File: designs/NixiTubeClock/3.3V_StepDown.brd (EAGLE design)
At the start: 31 x 32 mm, 10 parts, among them IC1 TPS62160DGKR, J1 S2B-PH-SM4, J2 S2B-PH-SM4

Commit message: added parts for nixi clock final check during the week
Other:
- board size 31 x 32 mm -> 31 x 34 mm
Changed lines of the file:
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@@
 <setting verticaltext="up"/>
 </settings>
-<grid distance="1" unitdist="mm" unit="mm" style="lines" multiple="1" display="yes" altdistance="5" altunitdist="mil" altunit="mil"/>
+<grid distance="2" unitdist="mm" unit="mm" style="lines" multiple="1" display="yes" altdistance="5" altunitdist="mil" altunit="mil"/>
 <layers>
 <layer number="1" name="Top" color="4" fill="1" visible="yes" active="yes"/>
@@
 </layers>
 <board>
-<fusionsync huburn="a.cGVyc29uYWw6dWUyYTNmMDU1" projecturn="a.cGVyc29uYWw6dWUyYTNmMDU1IzIwMTgxMjEwMTY0OTQ5MjI2" f3durn="urn:adsk.wipprod:dm.lineage:qr5fd7wmTYGYkqGqhFxAAQ" pcbguid="ed1bca21-045a-418e-931a-820db0e3dc27" lastpulledtime="" lastsyncedchangeguid="ae491c87-77c9-2377-a230-266f3260ef8a"/>
+<fusionsync huburn="a.cGVyc29uYWw6dWUyYTNmMDU1" projecturn="a.cGVyc29uYWw6dWUyYTNmMDU1IzIwMTgxMjEwMTY0OTQ5MjI2" f3durn="urn:adsk.wipprod:dm.lineage:qr5fd7wmTYGYkqGqhFxAAQ" pcbguid="ed1bca21-045a-418e-931a-820db0e3dc27" lastpulledtime="" lastsyncedchangeguid="2cda2d61-7268-cf4c-ad3c-c233fa6ebd5d"/>
 <plain>
 <text x="3.58" y="7.825" size="0.6096" layer="25">C1</text>
-<text x="2.405" y="21.225" size="1.016" layer="25" ratio="20" rot="R90">Gnd</text>
-<text x="0.675" y="21.225" size="1.016" layer="25" ratio="20" rot="R90">IOUT</text>
-<text x="25.025" y="21.225" size="1.016" layer="25" ratio="20" rot="R90">Gnd</text>
-<text x="23.295" y="21.225" size="1.016" layer="25" ratio="20" rot="R90">VIN</text>
-<text x="8.755" y="3.945" size="0.6096" layer="25" ratio="20" rot="R90">VIN</text>
-<text x="11.295" y="3.945" size="0.6096" layer="25" ratio="20" rot="R90">GND</text>
-<text x="13.835" y="3.945" size="0.6096" layer="25" ratio="20" rot="R90">GND</text>
-<text x="16.375" y="3.945" size="0.6096" layer="25" ratio="20" rot="R90">IOUT</text>
+<text x="0.405" y="21.225" size="1.016" layer="25" ratio="20" rot="R90">Gnd</text>
+<text x="2.675" y="21.225" size="1.016" layer="25" ratio="20" rot="R90">IOUT</text>
+<text x="23.025" y="21.225" size="1.016" layer="25" ratio="20" rot="R90">Gnd</text>
+<text x="25.295" y="21.225" size="1.016" layer="25" ratio="20" rot="R90">VIN</text>
+<text x="8.755" y="3.945" size="1.016" layer="25" ratio="20" rot="R90">VIN</text>
+<text x="11.295" y="3.945" size="1.016" layer="25" ratio="20" rot="R90">GND</text>
+<text x="13.835" y="3.945" size="1.016" layer="25" ratio="20" rot="R90">GND</text>
+<text x="16.375" y="3.945" size="1.016" layer="25" ratio="20" rot="R90">IOUT</text>
 <rectangle x1="22.99481875" y1="15.91635" x2="23.13198125" y2="15.92905" layer="22"/>
 <rectangle x1="19.00701875" y1="15.92905" x2="19.04258125" y2="15.94175" layer="22"/>
@@
 <dimension x1="24" y1="30" x2="23.765" y2="0" x3="33.5" y3="15" textsize="1.778" layer="47" dtype="vertical"/>
 <dimension x1="0" y1="1" x2="12.5" y2="2" x3="6.25" y3="-3.5" textsize="1.778" layer="47" dtype="horizontal"/>
-<hole x="0" y="2.5" drill="2.8"/>
-<hole x="25" y="2.5" drill="2.8"/>
+<hole x="0" y="0.5" drill="2.8"/>
+<hole x="25" y="0.5" drill="2.8"/>
 <hole x="0" y="27.5" drill="2.8"/>
 <hole x="25" y="27.5" drill="2.8"/>
@@
 <wire x1="22.5" y1="31" x2="26" y2="31" width="0.0762" layer="20"/>
 <wire x1="26" y1="31" x2="28" y2="29" width="0.0762" layer="20" curve="-90"/>
-<wire x1="28" y1="29" x2="28" y2="1" width="0.0762" layer="20"/>
-<wire x1="28" y1="1" x2="26" y2="-1" width="0.0762" layer="20" curve="-90"/>
-<wire x1="26" y1="-1" x2="-1" y2="-1" width="0.0762" layer="20"/>
-<wire x1="-1" y1="-1" x2="-3" y2="1" width="0.0762" layer="20" curve="-90"/>
-<wire x1="-3" y1="1" x2="-3" y2="29" width="0.0762" layer="20"/>
+<wire x1="28" y1="29" x2="28" y2="-1" width="0.0762" layer="20"/>
+<wire x1="28" y1="-1" x2="26" y2="-3" width="0.0762" layer="20" curve="-90"/>
+<wire x1="26" y1="-3" x2="-1" y2="-3" width="0.0762" layer="20"/>
+<wire x1="-1" y1="-3" x2="-3" y2="-1" width="0.0762" layer="20" curve="-90"/>
+<wire x1="-3" y1="-1" x2="-3" y2="29" width="0.0762" layer="20"/>
 <wire x1="-3" y1="29" x2="-1" y2="31" width="0.0762" layer="20" curve="-90"/>
 <wire x1="-1" y1="31" x2="2.5" y2="31" width="0.0762" layer="20"/>
@@
 <vertex x="7.3025" y="9.4375"/>
 <vertex x="9.39" y="7.35"/>
-<vertex x="9.39" y="-1"/>
+<vertex x="9.39" y="-3"/>
+<vertex x="-1" y="-3" curve="-90"/>
 <vertex x="-3" y="-1"/>
 </polygon>
@@
 <vertex x="13.335" y="9.12"/>
 <vertex x="15.24" y="7.215"/>
-<vertex x="15.24" y="-1"/>
+<vertex x="15.24" y="-3"/>
+<vertex x="26.0825" y="-3" curve="90"/>
 <vertex x="28.0825" y="-1"/>
 <vertex x="28.0825" y="31.3525"/>
@@
 <vertex x="7.9375" y="9.755"/>
 <vertex x="10.025" y="7.6675"/>
-<vertex x="10.025" y="-1"/>
-<vertex x="14.605" y="-1"/>
+<vertex x="10.025" y="-3"/>
+<vertex x="14.605" y="-3"/>
 <vertex x="14.605" y="6.8975"/>
 <vertex x="13.0175" y="8.485"/>
@@
 <vertex x="5.08" y="6.985"/>
 <vertex x="27.765" y="6.985"/>
-<vertex x="27.765" y="-1"/>
+<vertex x="27.765" y="-1" curve="-90"/>
+<vertex x="25.765" y="-3"/>
+<vertex x="-1" y="-3" curve="-90"/>
 <vertex x="-3" y="-1"/>
 <vertex x="-3" y="30.845"/>

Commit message: started work on mainboard
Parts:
- removed J1, J2: S2B-PH-SM4, CommonParts:JST_S2B-PH-SM4-TB(LF)(SN)
- moved C2 1.41 mm to (8.14, 17.0)
- moved C1 1.41 mm to (2.81, 12.0)
- moved IC1 1.41 mm to (8.14, 13.3)
- moved L1 1.41 mm to (19.5, 16.5)
- moved R1 1.41 mm to (18.8, 10.2)
- moved R2 1.41 mm to (14.0, 10.2)
- moved R3 1.41 mm to (10.4, 10.2)
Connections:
- net AGND: no longer J1.2, J2.2
- net IOUT: no longer J2.1
- net VIN: no longer J1.1
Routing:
- net VIN: track 52.6 -> 19.5 mm, vias 2 -> 0
- net AGND: track 55.0 -> 29.9 mm, vias 2 -> 0
- net IOUT: track 54.5 -> 48.6 mm
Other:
- board size 31 x 34 mm -> 26 x 28 mm
- board text removed: "Gnd"

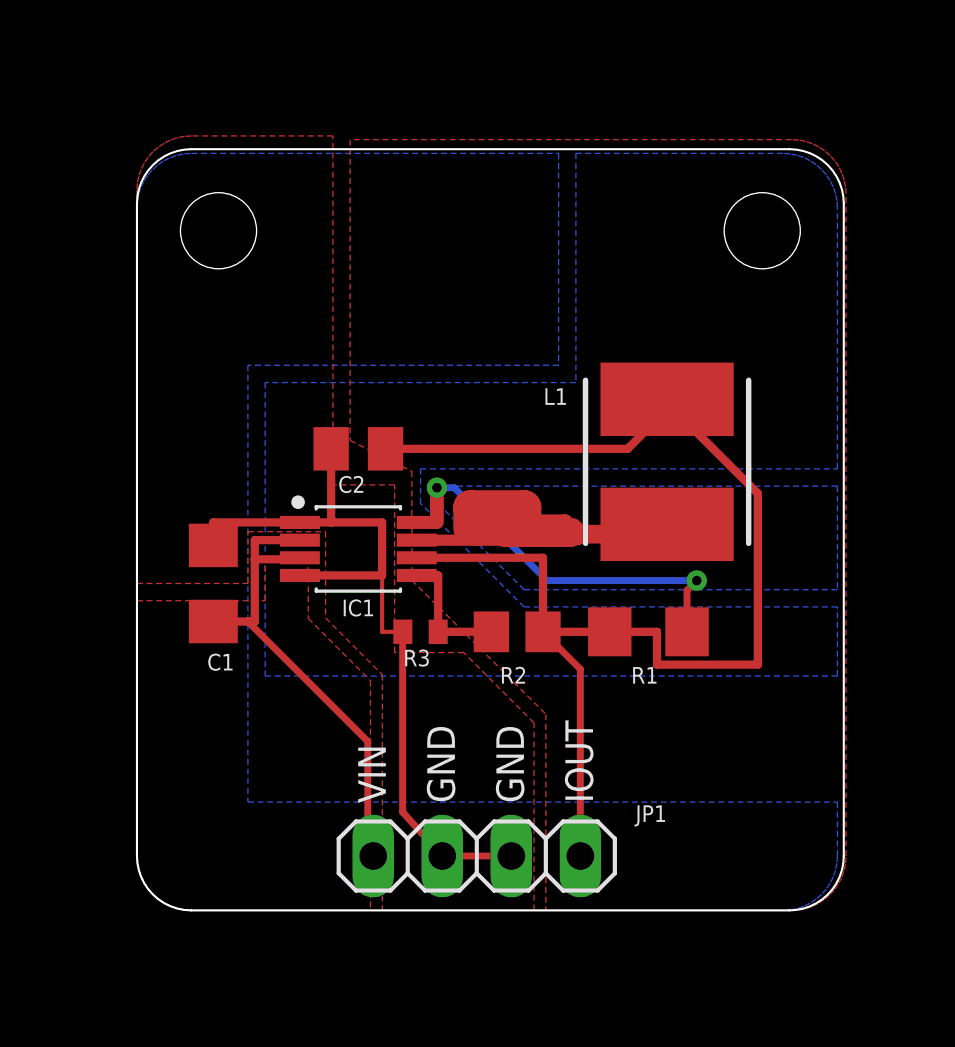
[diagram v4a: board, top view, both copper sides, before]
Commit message: added pinout on mainboard
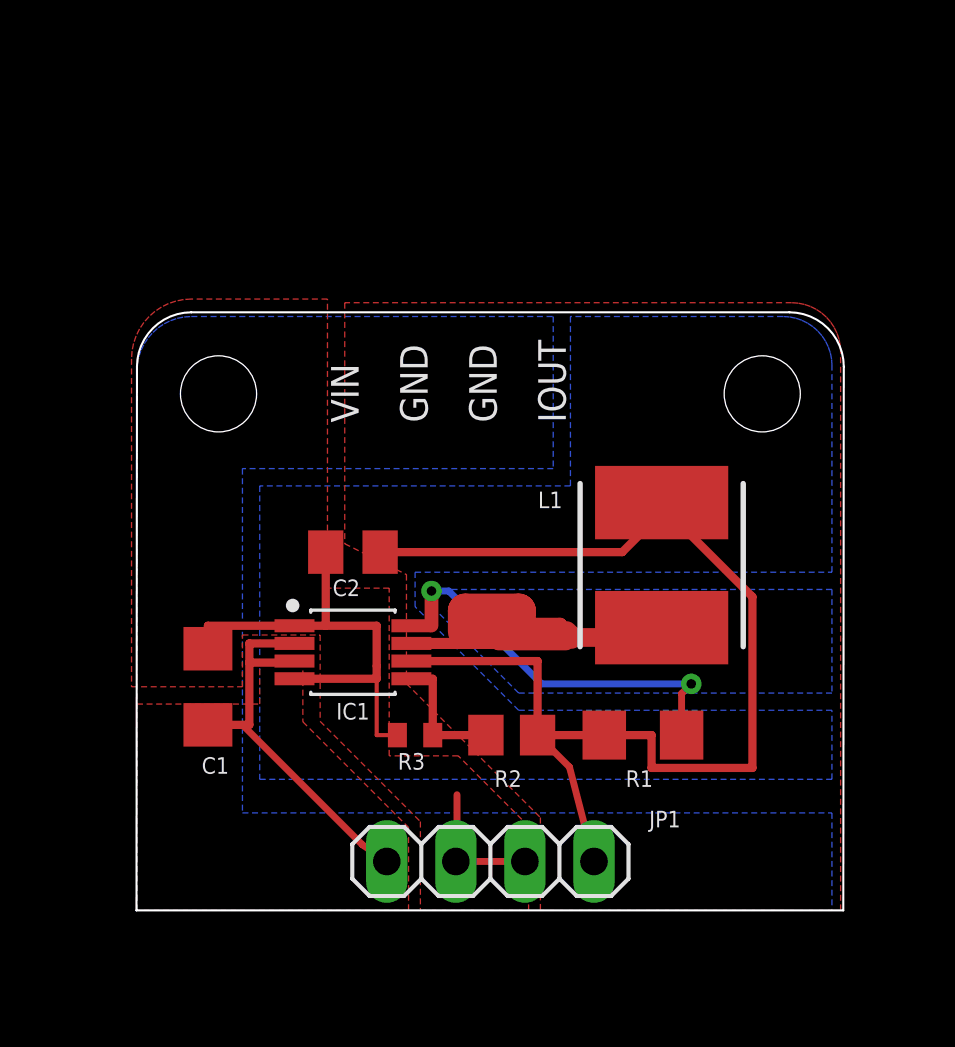
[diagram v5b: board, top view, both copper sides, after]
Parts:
- moved C1 3.81 mm to (2.61, 8.22)
- moved C2 3.81 mm to (7.94, 13.2)
- moved IC1 3.81 mm to (7.94, 9.49)
- moved L1 3.81 mm to (19.3, 12.7)
- moved R1 3.81 mm to (18.6, 6.45)
- moved R2 3.81 mm to (13.8, 6.45)
- moved R3 3.81 mm to (10.2, 6.45)
- moved JP1 0.54 mm to (13.0, 1.80)
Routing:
- net AGND: track 29.9 -> 23.6 mm
- net IOUT: track 48.6 -> 45.0 mm
- net VIN: track 19.5 -> 16.3 mm
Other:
- board size 26 x 28 mm -> 26 x 22 mm

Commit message: integrated T/H sensor
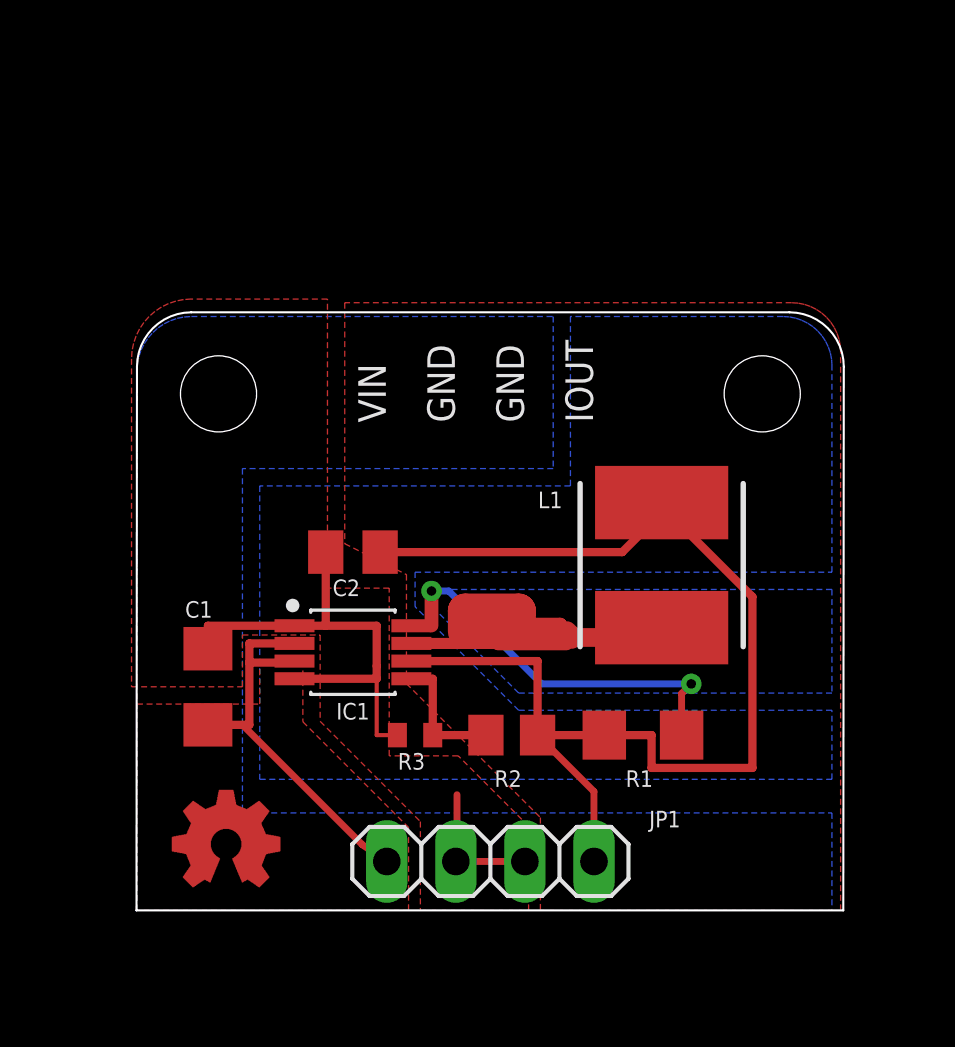
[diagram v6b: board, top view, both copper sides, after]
